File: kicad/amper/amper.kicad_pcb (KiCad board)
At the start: 2 copper layers, 100 x 100 mm, 56 parts, among them J1 Conn_02x05_Odd_Even, J2 Conn_02x05_Odd_Even, J3 Conn_02x05_Odd_Even, J4 USB_C_Receptacle_USB2.0, J5 Conn_01x03, J6 Conn_01x04, J7 Conn_01x05, Q1 FDS9435A, Q2 FDS9435A, SW1 SW_Push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

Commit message: Added some very cool segment routing if I do say so myself
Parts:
- moved C4 47.6 mm to (-19.0, -47.0), turned to 180 degrees
- moved C3 37.5 mm to (-25.0, -47.0)
- moved C5 35.4 mm to (-32.0, -43.0), turned to 180 degrees
- moved U1 14.1 mm to (-22.0, -39.0), turned to 270 degrees
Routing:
- net /SEG1: track 0.00 -> 152.5 mm, vias 0 -> 3
- net /SEG2: track 0.00 -> 147.9 mm, vias 0 -> 3
- net /SEG3: track 0.00 -> 142.7 mm, vias 0 -> 3
- net /SEG4: track 0.00 -> 137.7 mm, vias 0 -> 3
- net /SEG5: track 0.00 -> 123.7 mm, vias 0 -> 2
- net /SEG6: track 0.00 -> 118.5 mm, vias 0 -> 2
- net /SEG7: track 0.00 -> 116.3 mm, vias 0 -> 2
- net /SEG8: track 0.00 -> 113.1 mm, vias 0 -> 2
- net +5V: track 2.10 -> 7.71 mm
- net /SourceBDigit2: track 0.00 -> 2.00 mm
- net /SourceBDigit1: track 0.00 -> 2.00 mm
- net /SourceADigit2: track 0.00 -> 2.00 mm
- net /SourceADigit1: track 0.00 -> 2.00 mm
- net /OutDigit1: track 0.00 -> 2.00 mm

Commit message: Added grid routing
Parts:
- removed svg2mod: G***, amper:LargeOutput
- removed svg2mod: G***, amper:LargeB
- removed svg2mod: G***, amper:LargeA
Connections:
- U1 pad 10: /OutDigit2 -> /SourceADigit1
- U1 pad 11: /OutDigit1 -> /SourceADigit2
- U1 pad 12: /SourceBDigit2 -> /OutDigit1
- U1 pad 13: /SourceBDigit1 -> /OutDigit2
- U1 pad 14: /SourceADigit2 -> /SourceBDigit2
- U1 pad 15: /SourceADigit1 -> /SourceBDigit1
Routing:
- net /SourceBDigit2: track 2.00 -> 82.4 mm
- net /SourceBDigit1: track 2.00 -> 57.4 mm, vias 0 -> 2
- net /SourceADigit2: track 2.00 -> 53.6 mm, vias 0 -> 2
- net /OutDigit2: track 0.00 -> 43.5 mm, vias 0 -> 2
- net /SourceADigit1: track 2.00 -> 26.5 mm
- net /OutDigit1: track 2.00 -> 13.7 mm, vias 0 -> 2
- net GND: track 81.6 -> 89.7 mm
- net +5V: track 7.71 -> 3.04 mm

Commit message: Electrically connected, still needs some work
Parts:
- moved C1 55.0 mm to (-13.7, -39.5), turned to 90 degrees
- moved R5 49.0 mm to (-12.2, -39.5), turned to 270 degrees
- moved C2 47.4 mm to (-13.7, -43.5), turned to 270 degrees
- moved R6 44.5 mm to (-12.2, -43.5), turned to 90 degrees
- moved J6 14.5 mm to (33.5, -40.7)
- moved J5 14.5 mm to (33.5, -29.5)
- moved U7 13.0 mm to (19.5, -36.5)
- moved C12 12.1 mm to (19.5, -44.5)
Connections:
- C1 pad 2: /Tm1636Dio -> /Tm1637Dio
- C2 pad 2: /Tm1636Clk -> /Tm1637Clk
- R5 pad 1: /Tm1636Dio -> /Tm1637Dio
- R6 pad 1: /Tm1636Clk -> /Tm1637Clk
- U1 pad 17: /Tm1636Dio -> /Tm1637Dio
- U1 pad 18: /Tm1636Clk -> /Tm1637Clk
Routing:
- net /SourceAPwm: track 3.88 -> 109.8 mm, vias 0 -> 2
- net /ResultAdc: track 14.3 -> 101.9 mm, vias 0 -> 2
- net /SourceAOut: track 49.5 -> 132.3 mm, vias 2 -> 4
- net /SourceAUp: track 9.77 -> 89.7 mm, vias 0 -> 2
- net /SourceADn: track 9.77 -> 79.4 mm, vias 0 -> 2
- net /SourceBPwm: track 3.88 -> 72.6 mm, vias 0 -> 2
- net /SourceBOut: track 60.5 -> 126.4 mm, vias 2 -> 4
- net /SourceBDn: track 9.77 -> 67.2 mm, vias 0 -> 2
- net /SourceBUp: track 9.77 -> 64.8 mm, vias 0 -> 2
- net /Tm1637Dio: track 0.00 -> 34.4 mm
- net /Tm1637Clk: track 0.00 -> 33.3 mm
- net /UartTx: track 0.00 -> 22.0 mm, vias 0 -> 1
- net GND: track 89.7 -> 111.4 mm, vias 9 -> 17
- net /UartRx: track 0.00 -> 18.7 mm, vias 0 -> 1
- net /V-: track 0.00 -> 15.1 mm
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
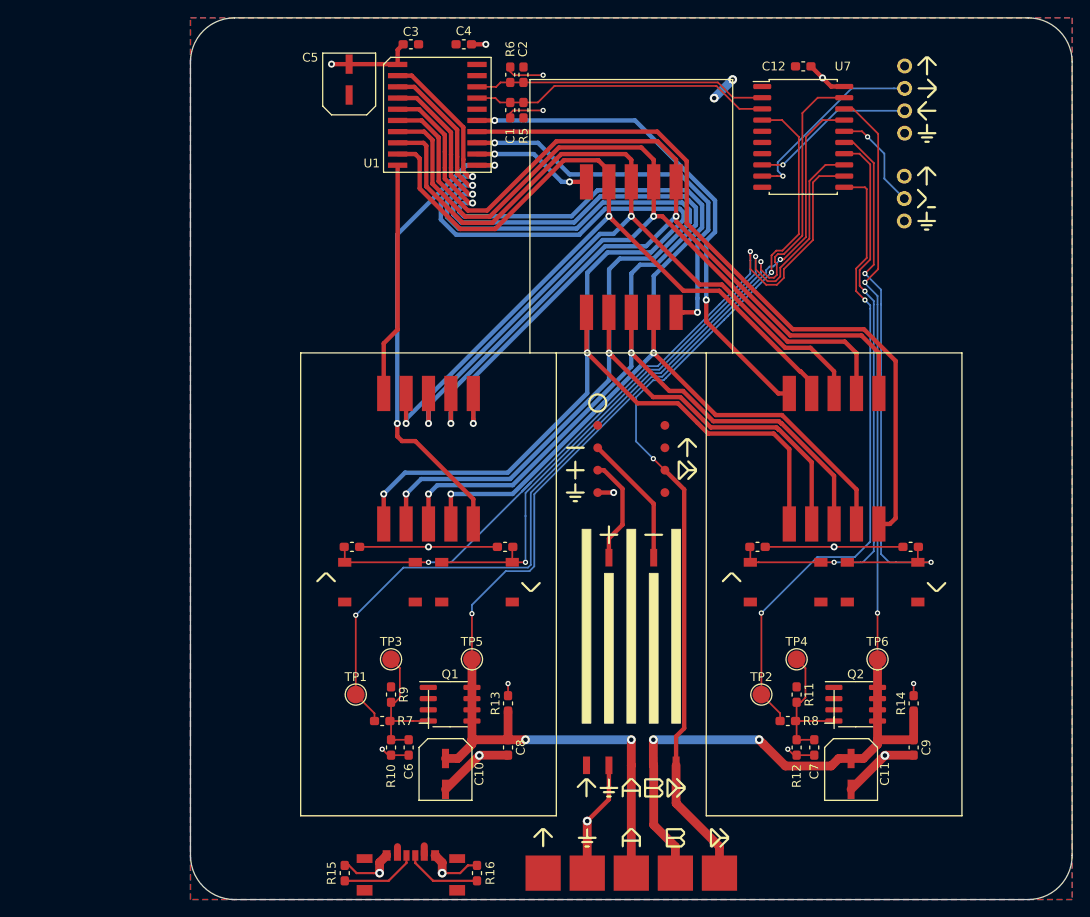
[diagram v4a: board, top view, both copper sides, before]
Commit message: almost finished first path at board rev b, still a little work to do around logos, text and plane continuity
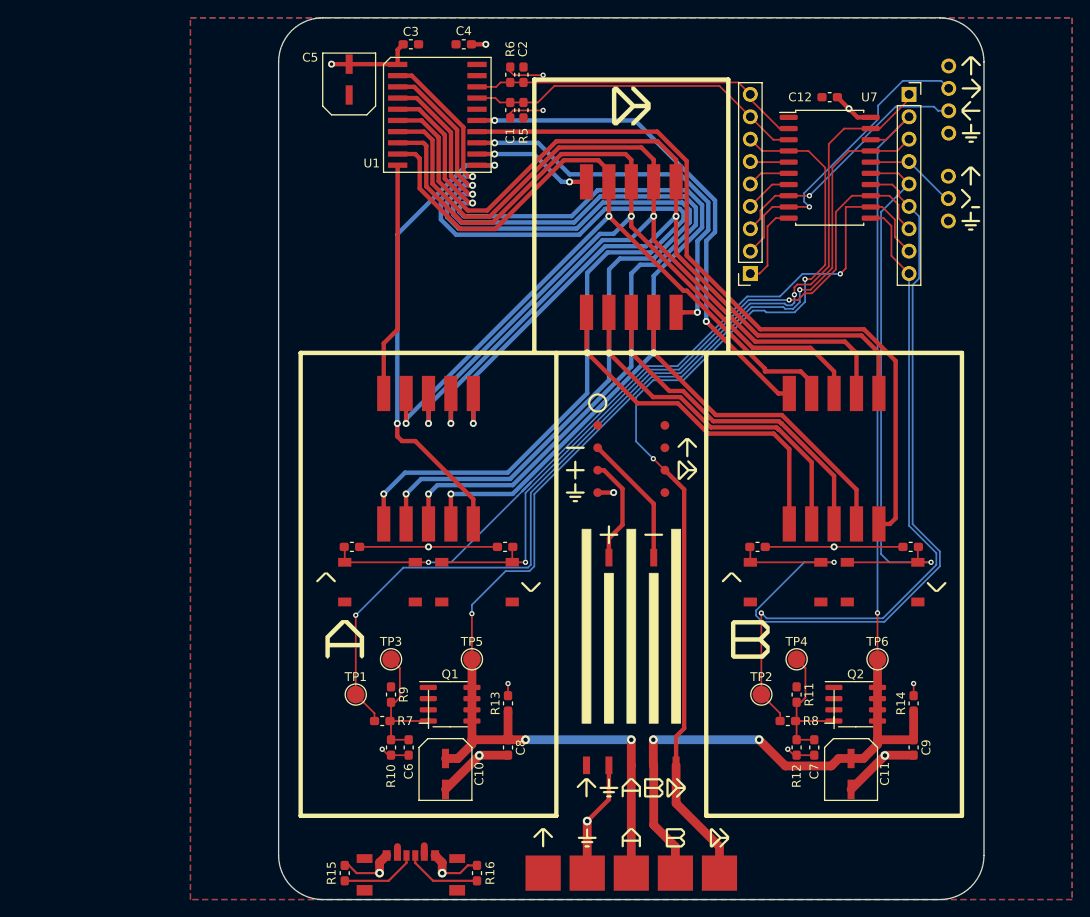
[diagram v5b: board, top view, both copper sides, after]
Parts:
- added J8: Conn_01x09, Connector_PinSocket_2.54mm:PinSocket_1x09_P2.54mm_Vertical, F.Cu at (13.5, -21.0)
- added J9: Conn_01x09, Connector_PinSocket_2.54mm:PinSocket_1x09_P2.54mm_Vertical, F.Cu at (31.5, -41.3)
- added svg2mod: G***, amper:LargeOutput, F.Cu at (0.00, -40.0)
- added svg2mod: G***, amper:LargeB, F.Cu at (13.5, 20.5)
- added svg2mod: G***, amper:LargeA, F.Cu at (-32.5, 20.5)
- moved J5 5.00 mm to (38.5, -29.5)
- moved J6 5.00 mm to (38.5, -40.7)
- moved C12 4.61 mm to (22.5, -41.0)
- moved U7 4.61 mm to (22.5, -33.0)
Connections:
- J4 pad S2: (no net) -> Net-(J4-PadS2)
- J4 pad S3: (no net) -> Net-(J4-PadS3)
- J4 pad S4: (no net) -> Net-(J4-PadS4)
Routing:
- net /SourceBUp: track 64.8 -> 95.3 mm, vias 2 -> 1
- net /UartTx: track 22.0 -> 35.0 mm
- net /UartRx: track 18.7 -> 29.2 mm
- net Net-(J8-Pad1): track 0.00 -> 9.56 mm
- net /SourceAOut: track 132.3 -> 139.5 mm
- net /ResultAdc: track 101.9 -> 108.9 mm
- net /SourceBPwm: track 72.6 -> 79.0 mm, vias 2 -> 1
- net Net-(J8-Pad4): track 0.00 -> 5.38 mm
- net Net-(J8-Pad5): track 0.00 -> 4.85 mm
- net /Tm1637Clk: track 33.3 -> 38.0 mm
- net /SourceAPwm: track 109.8 -> 114.5 mm
- net /Tm1637Dio: track 34.4 -> 38.9 mm
- net Net-(J8-Pad6): track 0.00 -> 4.38 mm
- net /SourceBOut: track 126.4 -> 130.0 mm, vias 4 -> 3
- net /SourceADn: track 79.4 -> 82.9 mm
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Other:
- board size 100 x 100 mm -> 80 x 100 mm

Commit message: Fixed a few issues, Ready for checking stage
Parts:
- added svg2mod: G***, amper:pcb_logo_small, B.Cu at (0.00, 20.0)
- moved C1 9.66 mm to (-17.2, -30.5)
- moved C2 9.66 mm to (-17.2, -34.5)
- moved C3 9.66 mm to (-28.5, -38.0)
- moved C4 9.66 mm to (-22.5, -38.0)
- moved C5 9.66 mm to (-35.5, -34.0)
- moved R5 9.66 mm to (-15.7, -30.5)
- moved R6 9.66 mm to (-15.7, -34.5)
- moved U1 9.66 mm to (-25.5, -30.0)
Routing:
- net /SEG6: track 120.0 -> 104.7 mm
- net /SEG5: track 125.9 -> 110.5 mm
- net /SEG7: track 114.9 -> 100.0 mm
- net /SEG8: track 108.3 -> 96.2 mm
- net /SourceADigit2: track 53.6 -> 43.1 mm
- net /SourceADigit1: track 26.5 -> 17.7 mm
- net /SEG4: track 137.7 -> 145.1 mm
- net /SEG3: track 142.7 -> 150.1 mm
- net /SEG1: track 152.5 -> 159.8 mm
- net /SEG2: track 147.9 -> 155.3 mm
- net /Tm1637Clk: track 38.0 -> 44.7 mm
- net /SourceBDigit1: track 58.9 -> 63.7 mm
- net /OutDigit1: track 13.7 -> 18.3 mm
- net /OutDigit2: track 44.4 -> 48.9 mm
- net /SourceBDigit2: track 84.5 -> 89.0 mm
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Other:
- board size 80 x 100 mm -> 80 x 99 mm
- board text added: "Amper Rev B"
